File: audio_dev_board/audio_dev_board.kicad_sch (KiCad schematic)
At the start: 34 parts, among them J1 TC2030, J2 USB_C_Receptacle_USB2.0_16P, SW1 SW_Push, U1 STM32H743VITx, U2 AMS1117-3.3, U3 USBLC6-2SC6, X1 25Mhz, X2 32kHz768

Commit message: ueiuei
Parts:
- removed C1: 10u, symbol Device:C
- removed C10, C20: 1u, symbol Device:C
- removed C11, C12, C19, C3, C4, C5, C6, C7, C9: 100n, symbol Device:C
- removed C13, C14, C15, C16: C, symbol Device:C
- removed C17, C18: 2u2, symbol Device:C
- removed C2: 22u, symbol Device:C
- removed C8: 4.7u, symbol Device:C
- removed F1: Polyfuse, symbol Device:Polyfuse
- removed FB1: FerriteBead, symbol Device:FerriteBead
- removed J1: TC2030, Connector:Tag-Connect_TC2030-IDC-FP_2x03_P1.27mm_Vertical, symbol Connector:Conn_ARM_SWD_TagConnect_TC2030
- removed J2: USB_C_Receptacle_USB2.0_16P, symbol Connector:USB_C_Receptacle_USB2.0_16P
- removed R1, R2: 5k1, symbol Device:R
- removed R3, R4: R, symbol Device:R
- removed SW1: SW_Push, symbol Switch:SW_Push
- removed U1: STM32H743VITx, Package_QFP:LQFP-100_14x14mm_P0.5mm, symbol MCU_ST_STM32H7:STM32H743VITx
- removed U2: AMS1117-3.3, Package_TO_SOT_SMD:SOT-223-3_TabPin2, symbol Regulator_Linear:AMS1117-3.3
- removed U3: USBLC6-2SC6, Package_TO_SOT_SMD:SOT-23-6, symbol Power_Protection:USBLC6-2SC6
- removed X1: 25Mhz, symbol Device:Crystal_GND24
- removed X2: 32kHz768, symbol Device:Crystal
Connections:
- no-connect marks 2 -> 0
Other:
- added sheet CODEC (CODEC.kicad_sch)
- added sheet MCU (MCU.kicad_sch)

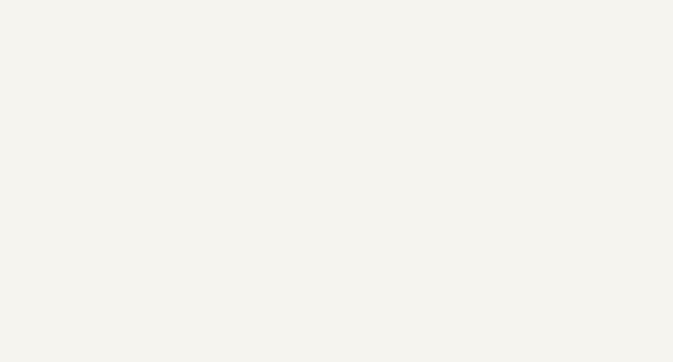
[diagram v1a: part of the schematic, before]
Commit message: added more scems
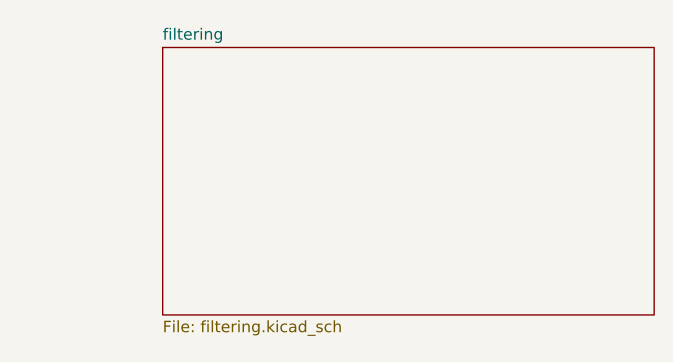
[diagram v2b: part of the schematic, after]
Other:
- added sheet filtering (filtering.kicad_sch)
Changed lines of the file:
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@@
+		)
+	)
+	(sheet
+		(at 216.408 43.688)
+		(size 54.61 29.718)
+		(fields_autoplaced yes)
+		(stroke
+			(width 0.1524)
+			(type solid)
+		)
+		(fill
+			(color 0 0 0 0.0000)
+		)
+		(property "Sheetname" "filtering"
+			(at 216.408 42.9764 0)
+			(effects
+				(font
+					(size 1.27 1.27)
+				)
+				(justify left bottom)
+			)
+		)
+		(property "Sheetfile" "filtering.kicad_sch"
+			(at 216.408 73.9906 0)
+			(effects
+				(font
+					(size 1.27 1.27)
+				)
+				(justify left top)
+			)
+		)
+		(instances
+			(project "audio_dev_board"
+				(path "/9f0c82f0-eba2-4eef-9ea0-d089929edc65"
+					(page "4")
+				)
+			)
 		)
 	)

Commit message: bluhhh
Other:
- added sheet Connectors (Connectors.kicad_sch)
- added sheet Power (Power.kicad_sch)
- sheet CODEC ports: added InputAFiltered, InputBFiltered, OutputRawA, OutputRawB; removed none
- sheet filtering ports: added InputFiltered, InputRaw, OutputProcessedA, OutputProcessedB, OutputRawA, OutputRawB; removed none
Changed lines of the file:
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@@
+	)
+	(sheet
+		(at 73.66 100.33)
+		(size 35.052 32.004)
+		(fields_autoplaced yes)
+		(stroke
+			(width 0.1524)
+			(type solid)
+		)
+		(fill
+			(color 0 0 0 0.0000)
+		)
+		(property "Sheetname" "Power"
+			(at 73.66 99.6184 0)
+			(effects
+				(font
+					(size 1.27 1.27)
+				)
+				(justify left bottom)
+			)
+		)
+		(property "Sheetfile" "Power.kicad_sch"
+			(at 73.66 132.9186 0)
+			(effects
+				(font
+					(size 1.27 1.27)
+				)
+				(justify left top)
+			)
+		)
+		(instances
+			(project "audio_dev_board"
+				(path "/9f0c82f0-eba2-4eef-9ea0-d089929edc65"
+					(page "6")
+				)
+			)
+		)
 	)
 	(sheet
@@
 	)
 	(sheet
+		(at 303.784 44.196)
+		(size 55.626 28.956)
+		(fields_autoplaced yes)
+		(stroke
+			(width 0.1524)
+			(type solid)
+		)
+		(fill
+			(color 0 0 0 0.0000)
+		)
+		(property "Sheetname" "Connectors"
+			(at 303.784 43.4844 0)
+			(effects
+				(font
+					(size 1.27 1.27)
+				)
+				(justify left bottom)
+			)
+		)
+		(property "Sheetfile" "Connectors.kicad_sch"
+			(at 303.784 73.7366 0)
+			(effects
+				(font
+					(size 1.27 1.27)
+				)
+				(justify left top)
+			)
+		)
+		(pin "OutputARaw" input
+			(at 303.784 63.5 180)
+			(effects
+				(font
+					(size 1.27 1.27)
+				)
+				(justify left)
+			)
+		)
+		(pin "OutputBRaw" input
+			(at 303.784 59.69 180)
+			(effects
+				(font
+					(size 1.27 1.27)
+				)
+				(justify left)
+			)
+		)
+		(pin "InputARaw" output
+			(at 303.784 55.88 180)
+			(effects
+				(font
+					(size 1.27 1.27)
+				)
+				(justify left)
+			)
+		)
+		(pin "InputBRaw" output
+			(at 303.784 52.07 180)
+			(effects
+				(font
+					(size 1.27 1.27)
+				)
+				(justify left)
+			)
+		)
+		(instances
+			(project "audio_dev_board"
+				(path "/9f0c82f0-eba2-4eef-9ea0-d089929edc65"
+					(page "5")
+				)
+			)
+		)
+	)
+	(sheet
 		(at 143.256 43.18)
 		(size 42.672 30.48)
@@
 				)
 				(justify left)
+			)
+		)
+		(pin "OutputRawA" output
+			(at 185.928 52.832 0)
+			(effects
+				(font
+					(size 1.27 1.27)
+				)
+				(justify right)
+			)
+		)
+		(pin "OutputRawB" output
+			(at 185.928 55.372 0)
+			(effects
+				(font
+					(size 1.27 1.27)
+				)
+				(justify right)
+			)
+		)
+		(pin "InputAFiltered" input
+			(at 185.928 57.912 0)
+			(effects
+				(font
+					(size 1.27 1.27)
+				)
+				(justify right)
+			)
+		)
+		(pin "InputBFiltered" input
+			(at 185.928 60.198 0)
+			(effects
+				(font
+					(size 1.27 1.27)
+				)
+				(justify right)
 			)
 		)
@@
 			)
 		)
+		(pin "OutputProcessedB" output
+			(at 216.408 60.198 180)
+			(effects
+				(font
+					(size 1.27 1.27)
+				)
+				(justify left)
+			)
+		)
+		(pin "OutputProcessedA" output
+			(at 216.408 57.404 180)
+			(effects
+				(font
+					(size 1.27 1.27)
+				)
+				(justify left)
+			)
+		)
+		(pin "InputRaw" input
+			(at 271.018 54.356 0)
+			(effects
+				(font
+					(size 1.27 1.27)
+				)
+				(justify right)
+			)
+		)
+		(pin "OutputRawA" input
+			(at 271.018 57.15 0)
+			(effects
+				(font
+					(size 1.27 1.27)
+				)
+				(justify right)
+			)
+		)
+		(pin "OutputRawB" input
+			(at 271.018 59.69 0)
+			(effects
+				(font
+					(size 1.27 1.27)
+				)
+				(justify right)
+			)
+		)
+		(pin "InputFiltered" output
+			(at 216.408 54.864 180)
+			(effects
+				(font
+					(size 1.27 1.27)
+				)
+				(justify left)
+			)
+		)
